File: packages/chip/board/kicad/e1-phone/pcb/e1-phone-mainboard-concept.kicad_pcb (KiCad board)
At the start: 2 copper layers, 64 x 132 mm, 0 parts

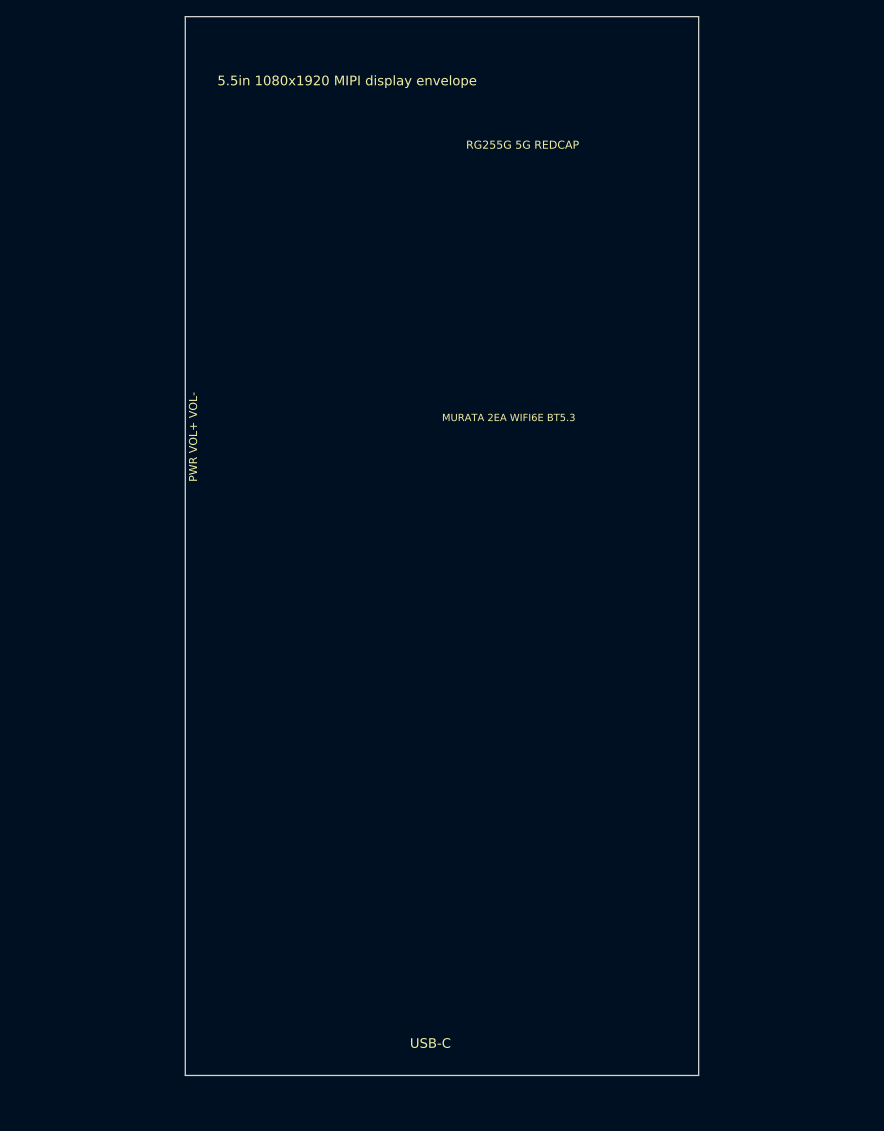
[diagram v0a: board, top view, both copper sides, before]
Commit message: Prepare chip package for publishing
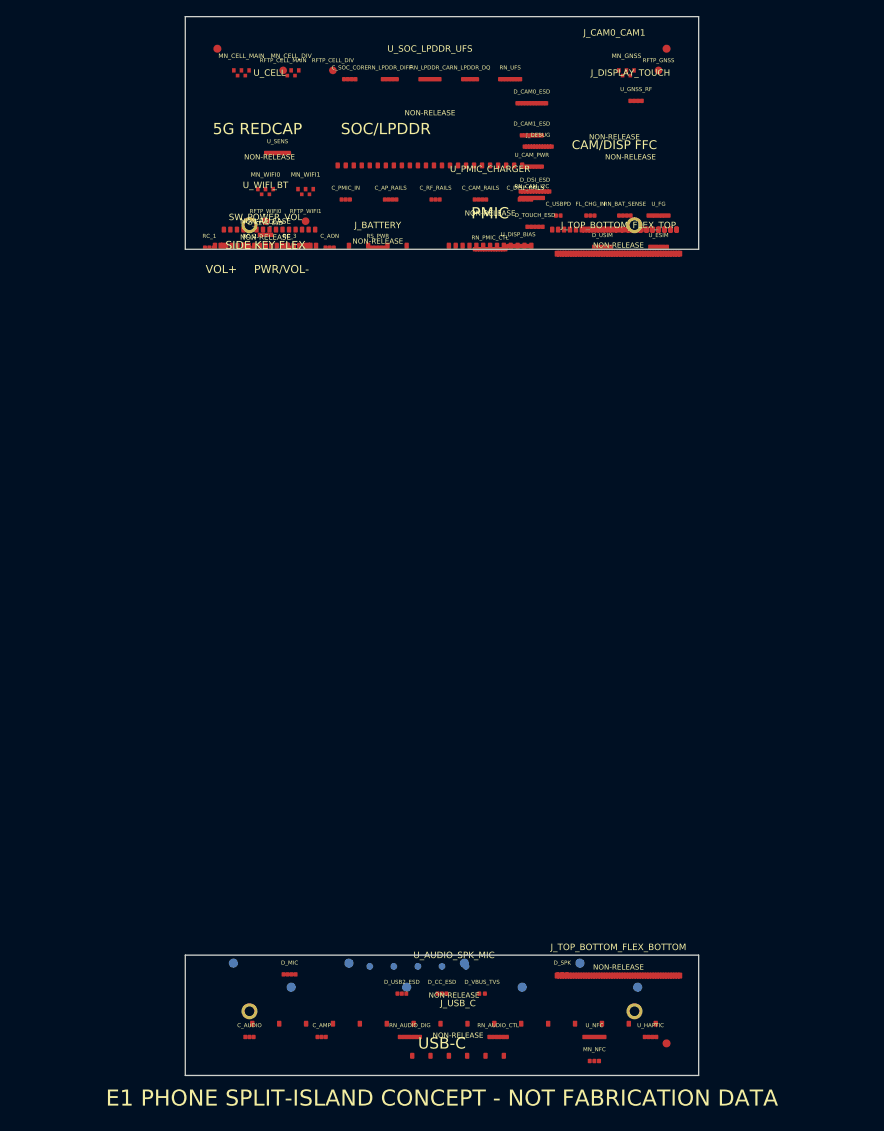
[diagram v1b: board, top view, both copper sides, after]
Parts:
- added C_AMP: SMART_AMP_RAIL_DECOUPLING, E1Phone:AUDIO_AMP_RAIL_DECOUPLING, F.Cu at (17.0, 127.2)
- added C_AON: AON_BUTTON_WAKE_DECOUPLING, E1Phone:POWER_AON_BUTTON_WAKE_DECOUPLING, F.Cu at (18.0, 28.8)
- added C_AP_RAILS: AP_CORE_IO_DECOUPLING, E1Phone:POWER_AP_RAIL_DECOUPLING, F.Cu at (25.6, 22.8)
- added C_AUDIO: AUDIO_CODEC_RAIL_DECOUPLING, E1Phone:AUDIO_CODEC_RAIL_DECOUPLING, F.Cu at (8.00, 127.2)
- added C_CAM_RAILS: CAMERA_AVDD_DVDD_DECOUPLING, E1Phone:POWER_CAMERA_RAIL_DECOUPLING, F.Cu at (36.8, 22.8)
- added C_DISP_RAILS: DISPLAY_BIAS_DECOUPLING, E1Phone:POWER_DISPLAY_RAIL_DECOUPLING, F.Cu at (42.4, 22.8)
- added C_PMIC_IN: PMIC_SYS_VBAT_INPUT_DECOUPLING, E1Phone:POWER_PMIC_INPUT_DECOUPLING, F.Cu at (20.0, 22.8)
- added C_RF_RAILS: RF_VBAT_IO_DECOUPLING, E1Phone:POWER_RF_RAIL_DECOUPLING, F.Cu at (31.2, 22.8)
- added C_SOC_CORE: SOC_CORE_IO_DECOUPLING, E1Phone:COMPUTE_SOC_LOCAL_DECOUPLING, F.Cu at (20.5, 7.80)
- added C_USBPD: USBPD_VIN_DECOUPLING, E1Phone:POWER_USBPD_LOCAL_RAIL, F.Cu at (46.5, 24.8)
- added D_CAM0_ESD: CAM0_CSI_ESD_ARRAY, E1Phone:CAMERA_CSI0_ESD, F.Cu at (43.2, 10.8)
- added D_CAM1_ESD: CAM1_CSI_ESD_ARRAY, E1Phone:CAMERA_CSI1_ESD, F.Cu at (43.2, 14.8)
- added D_CC_ESD: CC_ESD_ARRAY, E1Phone:USB_PROTECT_CC_ESD, F.Cu at (32.0, 121.8)
- added D_DSI_ESD: DSI_4LANE_ESD_ARRAY, E1Phone:DISPLAY_DSI_ESD, F.Cu at (43.6, 21.8)
- added D_KEYS_ESD: SIDE_KEY_ESD_ARRAY, E1Phone:SIDE_KEY_ESD, F.Cu at (10.0, 27.2)
- added D_MIC: PDM_MIC_ESD_BIAS_PLACEHOLDER, E1Phone:AUDIO_MIC_BIAS_ESD, F.Cu at (13.0, 119.4)
- added D_SPK: SPEAKER_OUTPUT_PROTECT, E1Phone:AUDIO_SPK_OUTPUT_PROTECT, F.Cu at (47.0, 119.4)
- added D_TOUCH_ESD: TOUCH_CONTROL_ESD, E1Phone:DISPLAY_TOUCH_CTRL_ESD, F.Cu at (43.6, 26.2)
- added D_USB2_ESD: USB2_ESD_ARRAY, E1Phone:USB_PROTECT_USB2_ESD, F.Cu at (27.0, 121.8)
- added D_USIM: USIM_ESD_LEVEL_SHIFT_PLACEHOLDER, E1Phone:PHONE_IDENTITY_USIM_ESD_LEVELSHIFT, F.Cu at (52.0, 28.7)
- added D_VBUS_TVS: VBUS_TVS, E1Phone:USB_PROTECT_VBUS_TVS, F.Cu at (37.0, 121.8)
- added FID_BR: FIDUCIAL, E1Phone:FID_BR, F.Cu at (60.0, 128.0)
- added FID_TL: FIDUCIAL, E1Phone:FID_TL, F.Cu at (4.00, 4.00)
- added FID_TR: FIDUCIAL, E1Phone:FID_TR, F.Cu at (60.0, 4.00)
- added FL_CHG_IN: VBUS_CHARGER_INPUT_FILTER, E1Phone:POWER_CHARGER_INPUT_FILTER, F.Cu at (50.5, 24.8)
- added J_BATTERY: battery_pack_power_thermistor_id, E1Phone:J_BATTERY, F.Cu at (24.0, 28.0)
- added J_CAM0_CAM1: rear_and_front_mipi_csi_cameras, E1Phone:J_CAM0_CAM1, F.Cu at (53.5, 15.0)
- added J_DEBUG: JTAG_BOOT_STRAP_TEST_ACCESS, E1Phone:COMPUTE_DEBUG_BOOT_STRAPS, F.Cu at (44.0, 16.2)
- added J_DISPLAY_TOUCH: 5p5_in_fhd_mipi_display_touch, E1Phone:J_DISPLAY_TOUCH, F.Cu at (55.5, 17.5)
- added J_TOP_BOTTOM_FLEX_BOTTOM: bottom_mate_for_split_board_interconnect, E1Phone:J_TOP_BOTTOM_FLEX_BOTTOM, F.Cu at (54.0, 118.5)
- added J_TOP_BOTTOM_FLEX_TOP: top_mate_for_split_board_interconnect, E1Phone:J_TOP_BOTTOM_FLEX_TOP, F.Cu at (54.0, 28.5)
- added J_USB_C: charging_data_debug_single_usb_c_port, E1Phone:J_USB_C, F.Cu at (34.0, 127.0)
- added MH_BL: MOUNT, E1Phone:MH_BL, F.Cu at (8.00, 124.0)
- added MH_BR: MOUNT, E1Phone:MH_BR, F.Cu at (56.0, 124.0)
- added MH_TL: MOUNT, E1Phone:MH_TL, F.Cu at (8.00, 26.0)
- added MH_TR: MOUNT, E1Phone:MH_TR, F.Cu at (56.0, 26.0)
- added MN_CELL_DIV: CELL_RF_DIV_PI_MATCH, E1Phone:RF_MATCH_CELL_RF_DIV, F.Cu at (13.2, 6.70)
- added MN_CELL_MAIN: CELL_RF_MAIN_PI_MATCH, E1Phone:RF_MATCH_CELL_RF_MAIN, F.Cu at (7.00, 6.70)
- added MN_GNSS: CELL_GNSS_RF_PI_MATCH, E1Phone:RF_MATCH_CELL_GNSS_RF, F.Cu at (55.0, 6.70)
- added MN_NFC: NFC_LOOP_MATCH_PLACEHOLDER, E1Phone:PHONE_IDENTITY_NFC_LOOP_MATCH, F.Cu at (51.0, 130.2)
- added MN_WIFI0: WIFI_BT_RF0_PI_MATCH, E1Phone:RF_MATCH_WIFI_BT_RF0, F.Cu at (10.0, 21.5)
- added MN_WIFI1: WIFI_BT_RF1_PI_MATCH, E1Phone:RF_MATCH_WIFI_BT_RF1, F.Cu at (15.0, 21.5)
- added RC_1: PWR_KEY_N_RC_DEBOUNCE, E1Phone:SIDE_KEY_COND_PWR_KEY_N, F.Cu at (3.00, 28.8)
- added RC_2: VOL_UP_N_RC_DEBOUNCE, E1Phone:SIDE_KEY_COND_VOL_UP_N, F.Cu at (8.00, 28.8)
- added RC_3: VOL_DOWN_N_RC_DEBOUNCE, E1Phone:SIDE_KEY_COND_VOL_DOWN_N, F.Cu at (13.0, 28.8)
- added RFTP_CELL_DIV: CELL_RF_DIV, E1Phone:RF_TP_CELL_RF_DIV, F.Cu at (18.4, 6.70)
- added RFTP_CELL_MAIN: CELL_RF_MAIN, E1Phone:RF_TP_CELL_RF_MAIN, F.Cu at (12.2, 6.70)
- added RFTP_GNSS: CELL_GNSS_RF, E1Phone:RF_TP_CELL_GNSS_RF, F.Cu at (59.0, 6.70)
- added RFTP_WIFI0: WIFI_BT_RF0, E1Phone:RF_TP_WIFI_BT_RF0, F.Cu at (10.0, 25.5)
- added RFTP_WIFI1: WIFI_BT_RF1, E1Phone:RF_TP_WIFI_BT_RF1, F.Cu at (15.0, 25.5)
- added RN_AUDIO_CTL: AUDIO_I2C_IRQ_PULLUPS, E1Phone:AUDIO_I2C_IRQ_PULLUPS, F.Cu at (39.0, 127.2)
- added RN_AUDIO_DIG: I2S_PDM_DAMPING_PLACEHOLDER, E1Phone:AUDIO_I2S_PDM_DAMPING, F.Cu at (28.0, 127.2)
- added RN_BAT_SENSE: BATTERY_NTC_ID_SENSE, E1Phone:POWER_CHARGER_BATTERY_SENSE, F.Cu at (54.8, 24.8)
- added RN_CAM_I2C: CAMERA_I2C_AF_PULLUPS, E1Phone:CAMERA_I2C_AF_PULLUPS, F.Cu at (43.2, 22.6)
- added RN_LPDDR_CA: LPDDR_CA_DAMPING_PLACEHOLDER, E1Phone:COMPUTE_LPDDR_CA_DAMPING, F.Cu at (30.5, 7.80)
- added RN_LPDDR_DIFF: LPDDR_CK_DQS_TERM_PLACEHOLDER, E1Phone:COMPUTE_LPDDR_CK_DQS_TERM, F.Cu at (25.5, 7.80)
- added RN_LPDDR_DQ: LPDDR_DQ_ESCAPE_PLACEHOLDER, E1Phone:COMPUTE_LPDDR_DQ_ESCAPE, F.Cu at (35.5, 7.80)
- added RN_PMIC_CTL: PMIC_CHARGER_PD_I2C_IRQ_PULLUPS, E1Phone:POWER_PMIC_CONTROL_PULLUPS, F.Cu at (38.0, 29.0)
- added RN_UFS: UFS_MPHY_ESD_TERM_PLACEHOLDER, E1Phone:COMPUTE_UFS_MPHY_ESD_TERM, F.Cu at (40.5, 7.80)
- added RS_PWR: VBUS_VBAT_SYS_CURRENT_SENSE, E1Phone:POWER_HIGH_CURRENT_SHUNT_PLACEHOLDERS, F.Cu at (24.0, 28.8)
- added SW_POWER_VOL: power_volume_side_key_flex_connector, E1Phone:SW_POWER_VOL, F.Cu at (10.0, 27.5)
- added TP_AON_1V8: AON_1V8, E1Phone:TP_AON_1V8, B.Cu at (27.6, 121.0)
- added TP_CAM_AVDD_2V8: CAM_AVDD_2V8, E1Phone:TP_CAM_AVDD_2V8, B.Cu at (49.2, 118.0)
- added TP_DISP_AVDD_5V5: DISP_AVDD_5V5, E1Phone:TP_DISP_AVDD_5V5, B.Cu at (56.4, 121.0)
- added TP_IO_1V8: IO_1V8, E1Phone:TP_IO_1V8, B.Cu at (34.8, 118.0)
- added TP_RF_VBAT: RF_VBAT, E1Phone:TP_RF_VBAT, B.Cu at (42.0, 121.0)
- added TP_SYS: SYS, E1Phone:TP_SYS, B.Cu at (20.4, 118.0)
- added TP_VBAT: VBAT, E1Phone:TP_VBAT, B.Cu at (13.2, 121.0)
- added TP_VBUS: VBUS, E1Phone:TP_VBUS, B.Cu at (6.00, 118.0)
- added USBTP_CC1: USB_CC1, E1Phone:USB_TP_CC1, B.Cu at (26.0, 118.4)
- added USBTP_CC2: USB_CC2, E1Phone:USB_TP_CC2, B.Cu at (29.0, 118.4)
- added USBTP_DN: USB_DN, E1Phone:USB_TP_DN, B.Cu at (35.0, 118.4)
- added USBTP_DP: USB_DP, E1Phone:USB_TP_DP, B.Cu at (32.0, 118.4)
- added USBTP_VBUS: VBUS, E1Phone:USB_TP_VBUS, B.Cu at (23.0, 118.4)
- added U_AUDIO_SPK_MIC: speakers_microphones_audio_codec_haptics, E1Phone:U_AUDIO_SPK_MIC, F.Cu at (33.5, 122.0)
- added U_CAM_PWR: CAMERA_POWER_SEQUENCE_PLACEHOLDER, E1Phone:CAMERA_POWER_SEQUENCE, F.Cu at (43.2, 18.7)
- added U_CELL: cellular_5g_redcap_module, E1Phone:U_CELL, F.Cu at (10.5, 17.5)
- added U_DISP_BIAS: DISPLAY_BIAS_BACKLIGHT_PLACEHOLDER, E1Phone:DISPLAY_BIAS_BACKLIGHT, F.Cu at (41.5, 28.6)
- added U_ESIM: ESIM_MODULE_PLACEHOLDER, E1Phone:PHONE_IDENTITY_ESIM_PLACEHOLDER, F.Cu at (59.0, 28.7)
- added U_FG: FUEL_GAUGE_PLACEHOLDER, E1Phone:POWER_FUEL_GAUGE_PLACEHOLDER, F.Cu at (59.0, 24.8)
- added U_GNSS_RF: GNSS_LNA_SAW_PLACEHOLDER, E1Phone:PHONE_IDENTITY_GNSS_LNA_SAW, F.Cu at (56.2, 10.5)
- added U_HAPTIC: HAPTIC_DRIVER_PLACEHOLDER, E1Phone:HAPTIC_DRIVER_OUTPUT, F.Cu at (58.0, 127.2)
- added U_NFC: NFC_CONTROLLER_PLACEHOLDER, E1Phone:PHONE_IDENTITY_NFC_CONTROLLER, F.Cu at (51.0, 127.2)
- added U_PMIC_CHARGER: pmic_charger_power_path, E1Phone:U_PMIC_CHARGER, F.Cu at (38.0, 24.5)
- added U_SENS: IMU_ALS_PROX_BARO_PLACEHOLDER, E1Phone:PHONE_IDENTITY_SENSOR_HUB, F.Cu at (11.5, 17.0)
- added U_SOC_LPDDR_UFS: compute_memory_storage, E1Phone:U_SOC_LPDDR_UFS, F.Cu at (30.5, 12.0)
- added U_WIFI_BT: wifi_6e_bluetooth_module, E1Phone:U_WIFI_BT, F.Cu at (10.0, 25.5)
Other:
- outline, holes or cut-outs redrawn
- copper layers 2 -> 10
- net class E1Phone_AUDIO_CONTROL_AON added: clearance 0.100, trace_width 0.100, via_dia 0.250, via_drill 0.100
- net class E1Phone_LPDDR_LENGTH_MATCHED added: clearance 0.080, trace_width 0.080, via_dia 0.220, via_drill 0.100
- net class E1Phone_MIPI_DPHY_100R added: clearance 0.100, trace_width 0.100, via_dia 0.250, via_drill 0.100
- net class E1Phone_PCIE_85R added: clearance 0.100, trace_width 0.100, via_dia 0.250, via_drill 0.100
- net class E1Phone_POWER added: clearance 0.160, trace_width 0.300, via_dia 0.450, via_drill 0.200
- net class E1Phone_RF_50R added: clearance 0.250, trace_width 0.180, via_dia 0.300, via_drill 0.150
- net class E1Phone_SDIO_50R added: clearance 0.100, trace_width 0.100, via_dia 0.250, via_drill 0.100
- net class E1Phone_SIM_NFC_SENSOR added: clearance 0.100, trace_width 0.100, via_dia 0.250, via_drill 0.100
- net class E1Phone_UFS_MPHY added: clearance 0.090, trace_width 0.090, via_dia 0.240, via_drill 0.100
- net class E1Phone_USB2_90R added: clearance 0.130, trace_width 0.120, via_dia 0.300, via_drill 0.150
- board text added: "5G REDCAP"
- board text added: "BATTERY CAVITY 64x87mm - TOP/BOTTOM ISLANDS"
- board text added: "CAM/DISP FFC"
- board text added: "E1 PHONE SPLIT-ISLAND CONCEPT - NOT FABRICATION DATA"
- board text added: "MECH_KEEP_DISPLAY_FPC"
- board text added: "MECH_KEEP_HAPTIC_LRA"
- board text added: "MECH_KEEP_RF_BOTTOM"
- board text added: "MECH_KEEP_RF_TOP"
- board text added: "MECH_KEEP_SIDE_KEY_ACTUATOR"
- board text added: "MECH_KEEP_SIM_TRAY"
- board text added: "MECH_KEEP_USB_C_CAPTURE"
- board text added: "PMIC"
- board text added: "PWR/VOL-"
- board text added: "SIDE KEY FLEX"
- board text added: "SOC/LPDDR"
- board text added: "VOL+"
- board text removed: "5.5in 1080x1920 MIPI display envelope"
- board text removed: "BATTERY CAVITY 64x87"
- board text removed: "MURATA 2EA WIFI6E BT5.3"
- board text removed: "PWR VOL+ VOL-"
- board text removed: "RG255G 5G REDCAP"
